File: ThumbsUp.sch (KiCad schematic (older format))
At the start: 153 parts, among them IC1 RP2040, IC2 W25Q128JVSIM, J1 Conn_01x04_Male, J10 Raiser_Male, J11 Raiser_Female, J12 Raiser_Male, J13 Raiser_Female, J14 Raiser_Male, J15 Raiser_Female, J16 Raiser_Male, J17 Raiser_Female, J18 Raiser_Male, J19 52559-1233, J2 Conn_01x04_Male, J20 Conn_01x04_Female, J21 Conn_01x04_Female, J22 Conn_01x04_Female, J23 Conn_01x04_Female, J24 Conn_01x04_Male, J25 Conn_01x04_Male, J26 Conn_01x04_Male, J27 Conn_01x04_Male, J28 Conn_01x04_Female, J29 Conn_01x04_Female, J3 Conn_01x04_Female, J30 Conn_01x04_Female, J31 Conn_01x04_Female, J32 USB_C_Receptacle_USB2.0, J33 STX-3501-3N, J4 Conn_01x04_Male, J5 Conn_01x04_Female, J6 Conn_01x04_Male, J7 Conn_01x04_Male, J8 Conn_01x04_Male, J9 Raiser_Female, U1 NCP1117-3.3_SOT223, Y1 ABLS-12.000MHZ-B4-T

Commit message: Prepared the boards to be split
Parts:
- removed D1, D10, D11, D12, D13, D14, D15, D16, D17, D18, D19, D2, D20, D21, D22, D23, D24, D25, D26, D27, D28, D29, D3, D30, D31, D32, D33, D34, D35, D36, D37, D38, D39, D4, D40, D41, D42, D43, D44, D5, D6, D7, D8, D9: D_Small, Diode_SMD:D_SOD-123, symbol Device:D_Small
- removed J19: 52559-1233, 52559-1233:525591233, symbol ThumbsUp-rescue:52559-1233-52559-1233
- removed J33: STX-3501-3N, STX-3501-3N:STX35013N, symbol STX-3501-3N:STX-3501-3N
- removed R4, R5: 4.7k, Resistor_SMD:R_0805_2012Metric, symbol Device:R_Small
- added BOOTSEL2, RUN2: TL1016AAF220QG, TL1016AAF220QG:TL1016AAF220QG, symbol TL1016AAF220QG:TL1016AAF220QG
- added C18, C8: 10uF, Capacitor_SMD:C_0805_2012Metric, symbol Device:C_Small
- added C19, C23, C25, C26, C27, C28, C29, C30, C31, C32: 0.1uF, Capacitor_SMD:C_0805_2012Metric, symbol Device:C_Small
- added C20, C24: 1uF, Capacitor_SMD:C_0805_2012Metric, symbol Device:C_Small
- added C21, C22: 27pF, Capacitor_SMD:C_0805_2012Metric, symbol Device:C_Small
- added F2: Polyfuse, Fuse:Fuse_1206_3216Metric, symbol Device:Polyfuse
- added IC3: RP2040, RP2040:QFN40P700X700X90-57N-D, symbol RP2040:RP2040
- added IC4: W25Q128JVSIM, W25Q128JVSIM:SOIC127P790X216-8N, symbol W25Q128JVSIM:W25Q128JVSIM
- added J19, J34, J38, J40, J42, J44: Raiser_Female, Connector_PinSocket_2.54mm:PinSocket_1x04_P2.54mm_Vertical, symbol Connector:Conn_01x04_Female
- added J33, J35, J39, J41, J43, J45: Raiser_Male, Connector_PinHeader_2.54mm:PinHeader_1x04_P2.54mm_Vertical, symbol Connector:Conn_01x04_Male
- added J36, J?: STX-3501-3N, STX35013N, symbol STX-3501-3N:STX-3501-3N
- added J37: USB_C_Receptacle_USB2.0, Connector_USB:USB_C_Receptacle_Palconn_UTC16-G, symbol Connector:USB_C_Receptacle_USB2.0
- added R10, R11: 5.1k, Resistor_SMD:R_0805_2012Metric, symbol Device:R_Small
- added R12: 10k, Resistor_SMD:R_0805_2012Metric, symbol Device:R_Small
- added R13: DNF, Resistor_SMD:R_0805_2012Metric, symbol Device:R_Small
- added R14, R15: 27.4, Resistor_SMD:R_0805_2012Metric, symbol Device:R_Small
- added R16: 1k, Resistor_SMD:R_0805_2012Metric, symbol Device:R_Small
- added R4, R5: R, symbol Device:R
- added U2: NCP1117-3.3_SOT223, Package_TO_SOT_SMD:SOT-223-3_TabPin2, symbol Regulator_Linear:NCP1117-3.3_SOT223
- added Y2: ABLS-12.000MHZ-B4-T, ABLS-12.000MHZ-B4-T:HC%2f49US-(AT49)_1, symbol Device:Crystal
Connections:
- net +1V1: now also C24.1, C26.1, C28.1, IC3.23 (DVDD_1), IC3.45 (VREG_VOUT), IC3.50 (DVDD_2)
- net +3V3: now also C18.1, C19.1, C20.1, C23.1, C25.1, C27.1, C29.1, C30.1, C31.1, C32.1, IC3.1 (IOVDD_1), IC3.10 (IOVDD_2), IC3.22 (IOVDD_3), IC3.33 (IOVDD_4), IC3.42 (IOVDD_5), IC3.43 (ADC_AVDD), IC3.44 (VREG_VIN), IC3.48 (USB_VDD), IC3.49 (IOVDD_6), IC4.8 (VCC), R13.2, R4.2, R5.2, U2.2 (VO); no longer J18.1 (Pin_1)
- net +5V: now also C8.1, F2.1, U2.3 (VI)
- net COL0: now also IC3.35 (GPIO23); no longer J20.4 (Pin_4)
- net COL1: now also IC3.36 (GPIO24); no longer J20.3 (Pin_3)
- net COL2: now also IC3.37 (GPIO25); no longer J20.2 (Pin_2), MX10.1 (COL)
- net COL3: now also IC3.38 (GPIO26/ADC0); no longer J20.1 (Pin_1), MX14.1 (COL)
- net COL4: now also IC3.34 (GPIO22); no longer J4.1 (Pin_1), MX15.1 (COL), MX16.1 (COL), MX17.1 (COL)
- net COL5: now also IC3.39 (GPIO27/ADC1); no longer J4.4 (Pin_4), MX19.1 (COL), MX20.1 (COL), MX21.1 (COL)
- net COL6: now also IC3.5 (GPIO3); no longer J6.1 (Pin_1), MX23.1 (COL), MX24.1 (COL), MX25.1 (COL)
- net COL7: now also IC3.4 (GPIO2); no longer J6.4 (Pin_4), MX27.1 (COL), MX28.1 (COL), MX29.1 (COL)
- net COL8: now also IC3.6 (GPIO4); no longer J24.1 (Pin_1), MX34.1 (COL)
- net COL9: now also IC3.7 (GPIO5); no longer J24.2 (Pin_2), MX38.1 (COL)
- net COLA: now also IC3.8 (GPIO6); no longer J24.3 (Pin_3)
- net COLB: now also IC3.9 (GPIO7); no longer J24.4 (Pin_4)
- net GND: now also IC1.26 (RUN), J20.4 (Pin_4), J24.4 (Pin_4), J4.1 (Pin_1), J6.1 (Pin_1), MX10.1 (COL), MX14.1 (COL), MX15.1 (COL), MX16.1 (COL), MX17.1 (COL), MX19.1 (COL), MX20.1 (COL), MX21.1 (COL), MX23.1 (COL), MX24.1 (COL), MX25.1 (COL), MX27.1 (COL), MX28.1 (COL), MX29.1 (COL), MX34.1 (COL), MX38.1 (COL), BOOTSEL2.3, BOOTSEL2.4, C18.2, C19.2, C20.2, C21.2, C22.2, C23.2, C24.2, C25.2, C26.2, C27.2, C28.2, C29.2, C30.2, C31.2, C32.2, C8.2, IC3.19 (TESTEN), IC3.26 (RUN), IC3.57 (GND), IC4.4 (GND), J37.A1 (GND), J37.A12 (GND), J37.B1 (GND), J37.B12 (GND), J37.S1 (SHIELD), R10.2, R11.1, RUN2.3, RUN2.4, U2.1 (GND); no longer J18.4 (Pin_4)
- net ROW1: now also IC3.3 (GPIO1)
- net ROW2: now also IC3.41 (GPIO29/ADC3)
- net ROW3: now also IC3.40 (GPIO28/ADC2)
- net K_Y: now reaches MX23.2 (ROW)
- net K_U: now reaches MX27.2 (ROW)
- net K_H: now reaches MX24.2 (ROW)
- net K_J: now reaches MX28.2 (ROW)
- net K_N: now reaches MX25.2 (ROW)
- net K_M: now reaches MX29.2 (ROW)
- net at J1.4 (Pin_4), MX1.1 (COL), MX2.1 (COL)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: now also MX11.1 (COL), MX12.1 (COL), MX13.1 (COL), MX4.1 (COL), MX5.1 (COL), MX6.1 (COL), MX7.1 (COL), MX8.1 (COL), MX9.1 (COL)
- net K_WIN: now reaches MX10.2 (ROW)
- net K_LALT: now reaches MX14.2 (ROW)
- net K_R: now reaches MX15.2 (ROW)
- net K_T: now reaches MX19.2 (ROW)
- net K_F: now reaches MX16.2 (ROW)
- net K_G: now reaches MX20.2 (ROW)
- net K_V: now reaches MX17.2 (ROW)
- net K_B: now reaches MX21.2 (ROW)
- net K_D: now reaches J22.4 (Pin_4)
- net K_S: now reaches J22.3 (Pin_3)
- net K_A: now reaches J22.2 (Pin_2)
- net K_TAB: now reaches J22.1 (Pin_1)
- net K_LSFT: now reaches J4.2 (Pin_2)
- net K_LWR: now reaches J6.2 (Pin_2)
- net K_E: now reaches J21.4 (Pin_4)
- net K_W: now reaches J21.3 (Pin_3)
- net K_Q: now reaches J21.2 (Pin_2)
- net K_ESC: now reaches J21.1 (Pin_1)
- net K_C: now reaches J23.4 (Pin_4)
- net K_X: now reaches J23.3 (Pin_3)
- net K_Z: now reaches J23.2 (Pin_2)
- net K_LCTL: now reaches J23.1 (Pin_1)
- net at J28.4 (Pin_4), MX42.1 (COL), MX43.1 (COL)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: now also MX31.1 (COL), MX32.1 (COL), MX33.1 (COL), MX35.1 (COL), MX36.1 (COL), MX37.1 (COL), MX39.1 (COL), MX40.1 (COL), MX41.1 (COL)
- net K_RALT: now reaches MX34.2 (ROW)
- net K_MNU: now reaches MX38.2 (ROW)
- net K_K: now reaches J26.4 (Pin_4)
- net K_L: now reaches J26.3 (Pin_3)
- net K_SEMICOL: now reaches J26.2 (Pin_2)
- net K_ENT: now reaches J26.1 (Pin_1)
- net K_I: now reaches J25.4 (Pin_4)
- net K_O: now reaches J25.3 (Pin_3)
- net K_P: now reaches J25.2 (Pin_2)
- net K_BSPC: now reaches J25.1 (Pin_1)
- net K_COMM: now reaches J27.4 (Pin_4)
- net K_DOT: now reaches J27.3 (Pin_3)
- net K_SLASH: now reaches J27.2 (Pin_2)
- net K_RCTL: now reaches J27.1 (Pin_1)
- net at J3.1 (Pin_1), MX22.1 (COL): now also MX18.1 (COL)
- net at J3.3 (Pin_3): no longer MX18.1 (COL)
- net at J5.1 (Pin_1), MX30.1 (COL): now also MX26.1 (COL)
- net at J5.3 (Pin_3): no longer MX26.1 (COL)
- net at RUN1.1, RUN1.2: no longer IC1.26 (RUN)
- net GND-TOP: no longer names the net of J17.4 (Pin_4)
- net ROW0 renamed TX
- net TX: now also R4.1
- net SCL: no longer names the net of IC1.30 (GPIO19)
- net SCL: no longer J18.3 (Pin_3)
- net SCL-TOP: no longer names the net of J17.3 (Pin_3)
- net SDA: no longer names the net of IC1.29 (GPIO18)
- net SDA: no longer J18.2 (Pin_2)
- net SDA-TOP: no longer names the net of J17.2 (Pin_2)
- net VCC-TOP: no longer names the net of J17.1 (Pin_1)
- new net: IC3.47 (USB_DP), R14.1
- new net: IC3.46 (USB_DM), R15.1
- new net: C22.1, R16.2, Y2.1
- new net: BOOTSEL2.1, BOOTSEL2.2, R12.1
- new net: IC4.1 (~CS), R12.2, R13.1
- new net: F2.2, J37.A4 (VBUS), J37.A9 (VBUS), J37.B4 (VBUS), J37.B9 (VBUS)
- new net: RUN2.1, RUN2.2
- new net: J37.B5 (CC2), R11.2
- new net: J37.A5 (CC1), R10.1
- new net K_RSE: J4.4 (Pin_4)
- new net K_RSFT: J6.4 (Pin_4)
- new net RD+: J37.A6 (D+), J37.B6 (D+), R14.2
- new net RD-: J37.A7 (D-), J37.B7 (D-), R15.2
- new net RQSPI_SCLK: IC3.52 (QSPI_SCLK), IC4.6 (CLK)
- new net RQSPI_SD0: IC3.53 (QSPI_SD0), IC4.5 (DI_(IO0))
- new net RQSPI_SD1: IC3.55 (QSPI_SD1), IC4.2 (DO_(IO1))
- new net RQSPI_SD2: IC3.54 (QSPI_SD2), IC4.3 (~WP_(IO2))
- new net RQSPI_SD3: IC3.51 (QSPI_SD3), IC4.7 (~HOLD_OR_~/RESET_(IO3))
- new net RTX: IC3.2 (GPIO0), R5.1
- new net RXIN: C21.1, IC3.20 (XIN), Y2.2
- new net RXOUT: IC3.21 (XOUT), R16.1
- now unconnected: J1.1 (Pin_1), J1.2 (Pin_2), J1.3 (Pin_3), J28.1 (Pin_1), J28.2 (Pin_2), J28.3 (Pin_3)
- no-connect marks 46 -> 108
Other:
- note removed: "Pull-up for \nCirque Trackpad"
- moved on the sheet: BOOTSEL1, C1, C10, C11, C12, C13, C14, C15, C16, C17, C2, C3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

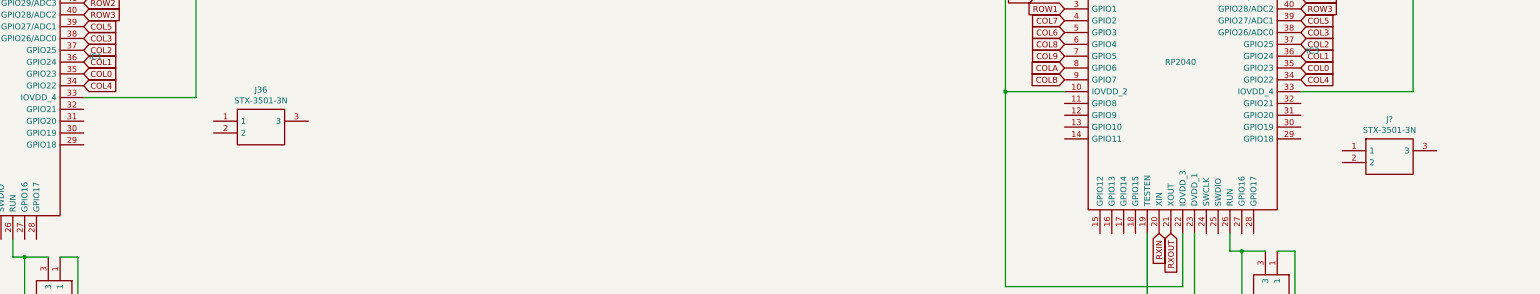
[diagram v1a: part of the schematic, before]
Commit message: Added audio connector
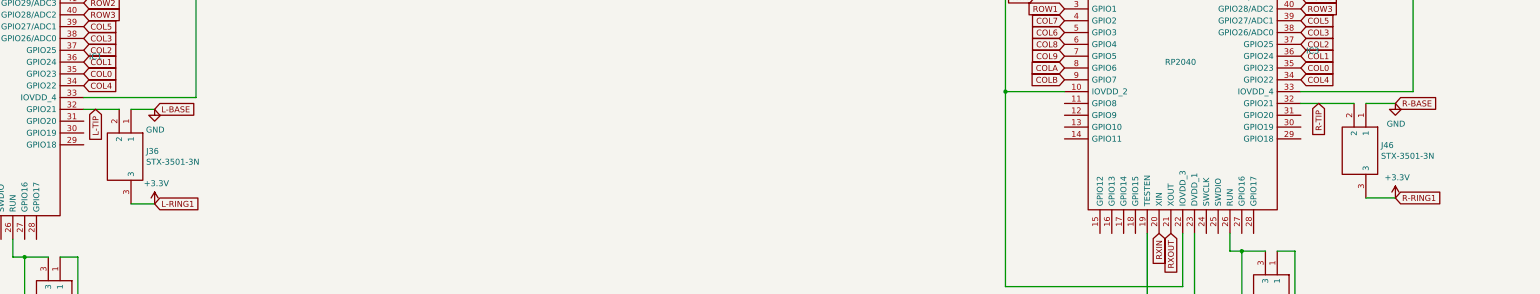
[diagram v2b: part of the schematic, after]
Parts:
- gave numbers to parts that had none: 1
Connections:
- net +3V3: now also J36.3, J46.3
- net GND: now also J36.1, J46.1
- net L-TIP: now reaches IC1.32 (GPIO21)
- net L-TIP: now also J36.2
- net R-TIP: now reaches IC3.32 (GPIO21)
- net R-TIP: now also J46.2
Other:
- moved on the sheet: J36, J46
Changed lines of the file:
@@
 Wire Wire Line
 	12300 7150 12400 7150
-$Comp
-L STX-3501-3N:STX-3501-3N J36
-U 1 1 63D573AD
-P 5350 8200
-F 0 "J36" H 5750 8465 50  0000 C CNN
-F 1 "STX-3501-3N" H 5750 8374 50  0000 C CNN
-F 2 "STX35013N" H 6000 8300 50  0001 L CNN
-F 3 "https://datasheet.datasheetarchive.com/originals/distributors/Datasheets_SAMA/ae9d1df0991347f2f81145ba35ca04dc.pdf" H 6000 8200 50  0001 L CNN
-F 4 "Phone Connectors 3.5mm S LUGS STEREO 3P THRU HOLE" H 6000 8100 50  0001 L CNN "Description"
-F 5 "5" H 6000 8000 50  0001 L CNN "Height"
-F 6 "Kycon" H 6000 7900 50  0001 L CNN "Manufacturer_Name"
-F 7 "STX-3501-3N" H 6000 7800 50  0001 L CNN "Manufacturer_Part_Number"
-F 8 "806-STX-3501-3N" H 6000 7700 50  0001 L CNN "Mouser Part Number"
-F 9 "https://www.mouser.co.uk/ProductDetail/Kycon/STX-3501-3N?qs=BBNwCsfFaznpJt4o1Jp%2FTg%3D%3D" H 6000 7600 50  0001 L CNN "Mouser Price/Stock"
-F 10 "" H 6000 7500 50  0001 L CNN "Arrow Part Number"
-F 11 "" H 6000 7400 50  0001 L CNN "Arrow Price/Stock"
-F 12 "" H 6000 7300 50  0001 L CNN "Mouser Testing Part Number"
-F 13 "" H 6000 7200 50  0001 L CNN "Mouser Testing Price/Stock"
-	1    5350 8200
-	1    0    0    -1
-$EndComp
 Wire Wire Line
 	2250 7200 2100 7200
@@
 NoConn ~ 21850 11250
 $Comp
-L STX-3501-3N:STX-3501-3N J?
+L STX-3501-3N:STX-3501-3N J46
 U 1 1 63F7C0D7
-P 14900 8450
-F 0 "J?" H 15300 8715 50  0000 C CNN
-F 1 "STX-3501-3N" H 15300 8624 50  0000 C CNN
-F 2 "STX35013N" H 15550 8550 50  0001 L CNN
-F 3 "https://datasheet.datasheetarchive.com/originals/distributors/Datasheets_SAMA/ae9d1df0991347f2f81145ba35ca04dc.pdf" H 15550 8450 50  0001 L CNN
-F 4 "Phone Connectors 3.5mm S LUGS STEREO 3P THRU HOLE" H 15550 8350 50  0001 L CNN "Description"
-F 5 "5" H 15550 8250 50  0001 L CNN "Height"
-F 6 "Kycon" H 15550 8150 50  0001 L CNN "Manufacturer_Name"
-F 7 "STX-3501-3N" H 15550 8050 50  0001 L CNN "Manufacturer_Part_Number"
-F 8 "806-STX-3501-3N" H 15550 7950 50  0001 L CNN "Mouser Part Number"
-F 9 "https://www.mouser.co.uk/ProductDetail/Kycon/STX-3501-3N?qs=BBNwCsfFaznpJt4o1Jp%2FTg%3D%3D" H 15550 7850 50  0001 L CNN "Mouser Price/Stock"
-F 10 "" H 15550 7750 50  0001 L CNN "Arrow Part Number"
-F 11 "" H 15550 7650 50  0001 L CNN "Arrow Price/Stock"
-F 12 "" H 15550 7550 50  0001 L CNN "Mouser Testing Part Number"
-F 13 "" H 15550 7450 50  0001 L CNN "Mouser Testing Price/Stock"
-	1    14900 8450
-	1    0    0    -1
-$EndComp
+P 15100 8050
+F 0 "J46" V 15454 8178 50  0000 L CNN
+F 1 "STX-3501-3N" V 15545 8178 50  0000 L CNN
+F 2 "STX35013N" H 15750 8150 50  0001 L CNN
+F 3 "https://datasheet.datasheetarchive.com/originals/distributors/Datasheets_SAMA/ae9d1df0991347f2f81145ba35ca04dc.pdf" H 15750 8050 50  0001 L CNN
+F 4 "Phone Connectors 3.5mm S LUGS STEREO 3P THRU HOLE" H 15750 7950 50  0001 L CNN "Description"
+F 5 "5" H 15750 7850 50  0001 L CNN "Height"
+F 6 "Kycon" H 15750 7750 50  0001 L CNN "Manufacturer_Name"
+F 7 "STX-3501-3N" H 15750 7650 50  0001 L CNN "Manufacturer_Part_Number"
+F 8 "806-STX-3501-3N" H 15750 7550 50  0001 L CNN "Mouser Part Number"
+F 9 "https://www.mouser.co.uk/ProductDetail/Kycon/STX-3501-3N?qs=BBNwCsfFaznpJt4o1Jp%2FTg%3D%3D" H 15750 7450 50  0001 L CNN "Mouser Price/Stock"
+F 10 "" H 15750 7350 50  0001 L CNN "Arrow Part Number"
+F 11 "" H 15750 7250 50  0001 L CNN "Arrow Price/Stock"
+F 12 "" H 15750 7150 50  0001 L CNN "Mouser Testing Part Number"
+F 13 "" H 15750 7050 50  0001 L CNN "Mouser Testing Price/Stock"
+	1    15100 8050
+	0    1    1    0
+$EndComp
+$Comp
+L STX-3501-3N:STX-3501-3N J36
+U 1 1 63D573AD
+P 4650 8100
+F 0 "J36" V 5004 8228 50  0000 L CNN
+F 1 "STX-3501-3N" V 5095 8228 50  0000 L CNN
+F 2 "STX35013N" H 5300 8200 50  0001 L CNN
+F 3 "https://datasheet.datasheetarchive.com/originals/distributors/Datasheets_SAMA/ae9d1df0991347f2f81145ba35ca04dc.pdf" H 5300 8100 50  0001 L CNN
+F 4 "Phone Connectors 3.5mm S LUGS STEREO 3P THRU HOLE" H 5300 8000 50  0001 L CNN "Description"
+F 5 "5" H 5300 7900 50  0001 L CNN "Height"
+F 6 "Kycon" H 5300 7800 50  0001 L CNN "Manufacturer_Name"
+F 7 "STX-3501-3N" H 5300 7700 50  0001 L CNN "Manufacturer_Part_Number"
+F 8 "806-STX-3501-3N" H 5300 7600 50  0001 L CNN "Mouser Part Number"
+F 9 "https://www.mouser.co.uk/ProductDetail/Kycon/STX-3501-3N?qs=BBNwCsfFaznpJt4o1Jp%2FTg%3D%3D" H 5300 7500 50  0001 L CNN "Mouser Price/Stock"
+F 10 "" H 5300 7400 50  0001 L CNN "Arrow Part Number"
+F 11 "" H 5300 7300 50  0001 L CNN "Arrow Price/Stock"
+F 12 "" H 5300 7200 50  0001 L CNN "Mouser Testing Part Number"
+F 13 "" H 5300 7100 50  0001 L CNN "Mouser Testing Price/Stock"
+	1    4650 8100
+	0    1    1    0
+$EndComp
+Wire Wire Line
+	4250 8100 4550 8100
+$Comp
+L power:GND #PWR?
+U 1 1 641658E3
+P 4850 8100
+F 0 "#PWR?" H 4850 7850 50  0001 C CNN
+F 1 "GND" H 4855 7927 50  0000 C CNN
+F 2 "" H 4850 8100 50  0001 C CNN
+F 3 "" H 4850 8100 50  0001 C CNN
+	1    4850 8100
+	1    0    0    -1
+$EndComp
+Wire Wire Line
+	4650 8100 4850 8100
+$Comp
+L power:+3.3V #PWR?
+U 1 1 641956AA
+P 4850 8900
+F 0 "#PWR?" H 4850 8750 50  0001 C CNN
+F 1 "+3.3V" H 4865 9073 50  0000 C CNN
+F 2 "" H 4850 8900 50  0001 C CNN
+F 3 "" H 4850 8900 50  0001 C CNN
+	1    4850 8900
+	1    0    0    -1
+$EndComp
+Wire Wire Line
+	4650 8900 4850 8900
+Text GLabel 4350 8100 3    50   Input ~ 0
+L-TIP
+Text GLabel 4850 8100 2    50   Input ~ 0
+L-BASE
+Text GLabel 4850 8900 2    50   Input ~ 0
+L-RING1
+Wire Wire Line
+	14550 8050 15000 8050
+$Comp
+L power:+3.3V #PWR?
+U 1 1 64225663
+P 15350 8850
+F 0 "#PWR?" H 15350 8700 50  0001 C CNN
+F 1 "+3.3V" H 15365 9023 50  0000 C CNN
+F 2 "" H 15350 8850 50  0001 C CNN
+F 3 "" H 15350 8850 50  0001 C CNN
+	1    15350 8850
+	1    0    0    -1
+$EndComp
+$Comp
+L power:GND #PWR?
+U 1 1 64226D4D
+P 15350 8050
+F 0 "#PWR?" H 15350 7800 50  0001 C CNN
+F 1 "GND" H 15355 7877 50  0000 C CNN
+F 2 "" H 15350 8050 50  0001 C CNN
+F 3 "" H 15350 8050 50  0001 C CNN
+	1    15350 8050
+	1    0    0    -1
+$EndComp
+Wire Wire Line
+	15100 8050 15350 8050
+Wire Wire Line
+	15100 8850 15350 8850
+Text GLabel 14700 8050 3    50   Input ~ 0
+R-TIP
+Text GLabel 15350 8050 2    50   Input ~ 0
+R-BASE
+Text GLabel 15350 8850 2    50   Input ~ 0
+R-RING1
 $EndSCHEMATC

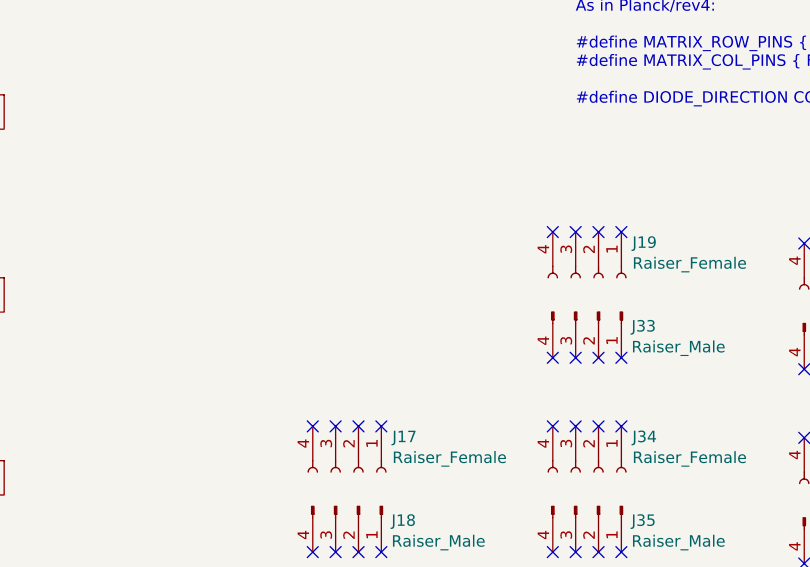
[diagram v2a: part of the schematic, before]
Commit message: Rearranged the header pins to match the actual positions.
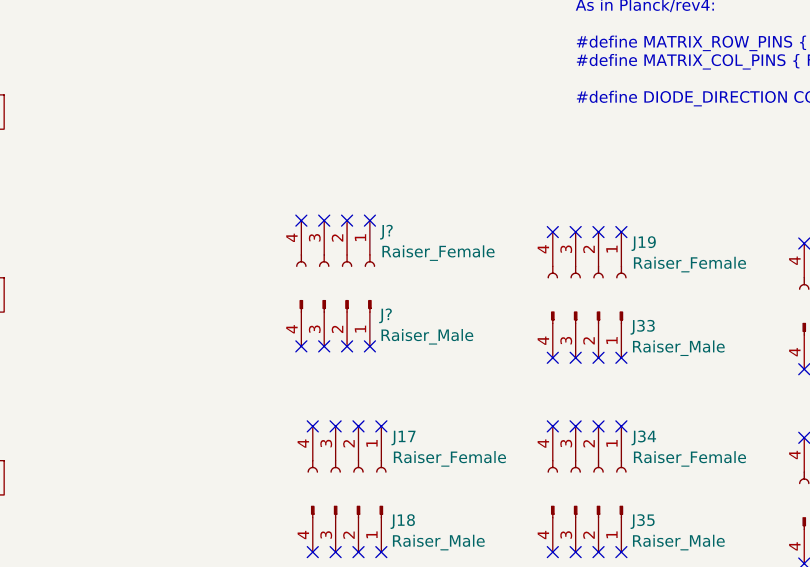
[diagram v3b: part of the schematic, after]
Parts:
- added J?: Raiser_Female, Connector_PinSocket_2.54mm:PinSocket_1x04_P2.54mm_Vertical, symbol Connector:Conn_01x04_Female
- added J?: Raiser_Male, Connector_PinHeader_2.54mm:PinHeader_1x04_P2.54mm_Vertical, symbol Connector:Conn_01x04_Male
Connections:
- no-connect marks 108 -> 116
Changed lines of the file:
@@
 	4250 8100 4550 8100
 $Comp
-L power:GND #PWR?
+L power:GND #PWR0149
 U 1 1 641658E3
 P 4850 8100
-F 0 "#PWR?" H 4850 7850 50  0001 C CNN
+F 0 "#PWR0149" H 4850 7850 50  0001 C CNN
 F 1 "GND" H 4855 7927 50  0000 C CNN
 F 2 "" H 4850 8100 50  0001 C CNN
@@
 	4650 8100 4850 8100
 $Comp
-L power:+3.3V #PWR?
+L power:+3.3V #PWR0150
 U 1 1 641956AA
 P 4850 8900
-F 0 "#PWR?" H 4850 8750 50  0001 C CNN
+F 0 "#PWR0150" H 4850 8750 50  0001 C CNN
 F 1 "+3.3V" H 4865 9073 50  0000 C CNN
 F 2 "" H 4850 8900 50  0001 C CNN
@@
 	14550 8050 15000 8050
 $Comp
-L power:+3.3V #PWR?
+L power:+3.3V #PWR0151
 U 1 1 64225663
 P 15350 8850
-F 0 "#PWR?" H 15350 8700 50  0001 C CNN
+F 0 "#PWR0151" H 15350 8700 50  0001 C CNN
 F 1 "+3.3V" H 15365 9023 50  0000 C CNN
 F 2 "" H 15350 8850 50  0001 C CNN
@@
 $EndComp
 $Comp
-L power:GND #PWR?
+L power:GND #PWR0152
 U 1 1 64226D4D
 P 15350 8050
-F 0 "#PWR?" H 15350 7800 50  0001 C CNN
+F 0 "#PWR0152" H 15350 7800 50  0001 C CNN
 F 1 "GND" H 15355 7877 50  0000 C CNN
 F 2 "" H 15350 8050 50  0001 C CNN
@@
 Text GLabel 15350 8850 2    50   Input ~ 0
 R-RING1
+$Comp
+L Connector:Conn_01x04_Female J?
+U 1 1 63AC0C46
+P 18150 12650
+F 0 "J?" V 17996 12798 50  0000 L CNN
+F 1 "Raiser_Female" V 18087 12798 50  0000 L CNN
+F 2 "Connector_PinSocket_2.54mm:PinSocket_1x04_P2.54mm_Vertical" H 18150 12650 50  0001 C CNN
+F 3 "~" H 18150 12650 50  0001 C CNN
+	1    18150 12650
+	0    1    1    0
+$EndComp
+$Comp
+L Connector:Conn_01x04_Male J?
+U 1 1 63AC0C4C
+P 18150 12800
+F 0 "J?" V 18212 12944 50  0000 L CNN
+F 1 "Raiser_Male" V 18303 12944 50  0000 L CNN
+F 2 "Connector_PinHeader_2.54mm:PinHeader_1x04_P2.54mm_Vertical" H 18150 12800 50  0001 C CNN
+F 3 "~" H 18150 12800 50  0001 C CNN
+	1    18150 12800
+	0    1    1    0
+$EndComp
+NoConn ~ 17950 12450
+NoConn ~ 18050 12450
+NoConn ~ 18150 12450
+NoConn ~ 18250 12450
+NoConn ~ 17950 13000
+NoConn ~ 18050 13000
+NoConn ~ 18150 13000
+NoConn ~ 18250 13000
 $EndSCHEMATC

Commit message: Reviewed the basic layout
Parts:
- gave numbers to parts that had none: 2
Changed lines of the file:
@@
 R-RING1
 $Comp
-L Connector:Conn_01x04_Female J?
+L Connector:Conn_01x04_Female J47
 U 1 1 63AC0C46
 P 18150 12650
-F 0 "J?" V 17996 12798 50  0000 L CNN
+F 0 "J47" V 17996 12798 50  0000 L CNN
 F 1 "Raiser_Female" V 18087 12798 50  0000 L CNN
 F 2 "Connector_PinSocket_2.54mm:PinSocket_1x04_P2.54mm_Vertical" H 18150 12650 50  0001 C CNN
@@
 $EndComp
 $Comp
-L Connector:Conn_01x04_Male J?
+L Connector:Conn_01x04_Male J48
 U 1 1 63AC0C4C
 P 18150 12800
-F 0 "J?" V 18212 12944 50  0000 L CNN
+F 0 "J48" V 18212 12944 50  0000 L CNN
 F 1 "Raiser_Male" V 18303 12944 50  0000 L CNN
 F 2 "Connector_PinHeader_2.54mm:PinHeader_1x04_P2.54mm_Vertical" H 18150 12800 50  0001 C CNN
